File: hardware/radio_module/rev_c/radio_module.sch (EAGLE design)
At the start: 139 parts, among them J1 MOLEX_73251-135X, J10 TC2030-JLINK-L, J11 TC2030-JLINK-NL, J12 U.FL-R-SMT, J13 U.FL-R-SMT, J2 MOLEX_73251-135X, J3 NANO_SIM, J7 SIGNPOST_DEBUG_HEADERSMT, J8 SIGNPOST_MODULE_HEADER, J9 TC2030-JLINK-NL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

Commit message: fixed digikey part numbers
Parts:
- C10, C11, C12: DIGIKEY 490-6241-1-ND -> 490-6241-1-ND
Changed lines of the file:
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@@
 </part>
 <part name="C10" library="passives" deviceset="CAPACITOR" device="0402_CAP" value="47pF">
-<attribute name="DIGIKEY" value="490-6241-1-ND "/>
+<attribute name="DIGIKEY" value="490-6241-1-ND"/>
 </part>
 <part name="C11" library="passives" deviceset="CAPACITOR" device="0402_CAP" value="47pF">
-<attribute name="DIGIKEY" value="490-6241-1-ND "/>
+<attribute name="DIGIKEY" value="490-6241-1-ND"/>
 </part>
 <part name="C12" library="passives" deviceset="CAPACITOR" device="0402_CAP" value="47pF">
-<attribute name="DIGIKEY" value="490-6241-1-ND "/>
+<attribute name="DIGIKEY" value="490-6241-1-ND"/>
 </part>
 <part name="GND6" library="umich" deviceset="GND" device=""/>

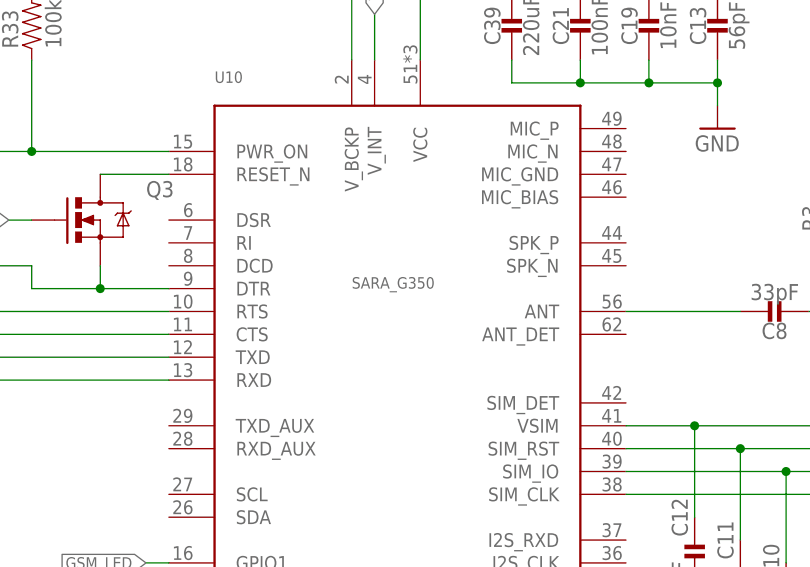
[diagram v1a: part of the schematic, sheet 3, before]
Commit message: added radio module with bom updates
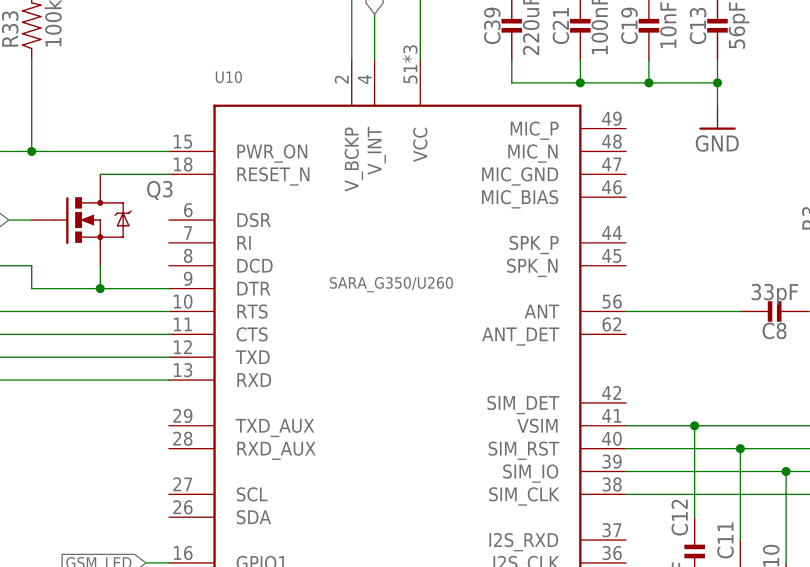
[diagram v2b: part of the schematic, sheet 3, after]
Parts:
- C1: DESCRIPTION (none) -> CAP CER 0.8PF 50V C0G/NP0 0402; MANUFACTURER (none) -> Murata; MPN (none) -> GRM1555C1HR80BA01D
- C10, C11, C12, C9: DESCRIPTION (none) -> CAP CER 47PF 50V C0G/NP0 0402; MANUFACTURER (none) -> Murata; MPN (none) -> GRM1555C1H470FA01D
- C13: DESCRIPTION (none) -> CAP CER 56PF 50V C0G/NP0 0402; DIGIKEY 490-1288-1-ND -> 490-1288-1-ND; MANUFACTURER (none) -> Murata; MPN (none) -> GRM1555C1H560JA01D
- C14, C15: DESCRIPTION (none) -> CAP CER 1000PF 50V X7R 0402; MANUFACTURER (none) -> Murata; MPN (none) -> GRM155R71H102KA01D
- C16: DESCRIPTION (none) -> CAP CER 2200PF 25V 10% X7R 0402; MANUFACTURER (none) -> Murata; MPN (none) -> GRM155R71E222KA01D
- C17, C18: DESCRIPTION (none) -> CAP CER 3300PF 50V 10% X7R 0402; MANUFACTURER (none) -> Murata; MPN (none) -> GRM155R71H332KA01D
- C19: DESCRIPTION (none) -> CAP CER 10000PF 50V 10% X7R 0402; DIGIKEY 490-4516-1-ND -> 490-4516-1-ND; MANUFACTURER (none) -> Murata; MPN (none) -> GRM155R71H103KA88D
- C2, C3: DESCRIPTION (none) -> CAP CER 8PF 50V C0G/NP0 0402; MANUFACTURER (none) -> Murata; MPN (none) -> GRM1555C1H8R0BA01D
- C20: DESCRIPTION (none) -> CAP CER 0.047UF 25V X7R 0402; MANUFACTURER (none) -> Murata; MPN (none) -> GRM155R71E473KA88D
- C21, C22, C23, C24, C25, C26, C27, C28, C29: DESCRIPTION (none) -> CAP CER 0.1UF 10V X7R 0402; MANUFACTURER (none) -> Murata; MPN (none) -> GRM155R71A104JA01D
- C30: DESCRIPTION (none) -> CAP CER 1UF 6.3V X5R 0402; MANUFACTURER (none) -> Murata; MPN (none) -> GRM155R60J105KE19D
- C31, C32: DESCRIPTION (none) -> CAP CER 4.7UF 10V X5R 0402; MANUFACTURER (none) -> Murata; MPN (none) -> ZRB15XR61A475KE01D
- C33, C34, C35: DESCRIPTION (none) -> CAP CER 10UF 6.3V X6S 0402; MANUFACTURER (none) -> Murata; MPN (none) -> GRM155C80J106ME11D
- C36, C37: DESCRIPTION (none) -> CAP CER 22UF 6.3V X5R 0402; DIGIKEY 1276-6834-1-ND -> 1276-6834-1-ND; MANUFACTURER (none) -> Samsung; MPN (none) -> CL05A226MQ5QUNC
- C38: DESCRIPTION (none) -> CAP CER 100UF 6.3V X5R 0805; MANUFACTURER (none) -> Murata; MPN (none) -> GRM21BR60J107ME15L
- C39: DESCRIPTION (none) -> CAP CER 220UF 6.3V X5R 1210; DIGIKEY 1276-3375-1-ND -> 1276-3375-1-ND; MANUFACTURER (none) -> Samsung; MPN (none) -> CL32A227MQVNNNE
- C4, C5, C6, C7: DESCRIPTION (none) -> CAP CER 12PF 50V C0G/NP0 0402; MANUFACTURER (none) -> Murata; MPN (none) -> GRM1555C1H120GA01D
- C8: DESCRIPTION (none) -> CAP CER 33PF 250V C0G/NP0 0603; MANUFACTURER (none) -> Johanson; MPN (none) -> 251R14S330JV4T
- D1, D2, D3, D4: DIGIKEY PESD0402-140CT-ND -> PESD0402-140CT-ND; MANUFACTURER (none) -> Littlefuse; MPN (none) -> PESD0402-140
- FB1: DESCRIPTION (none) -> FERRITE BEAD 1.5 KOHM 0402 1LN; MANUFACTURER (none) -> TDK; MPN (none) -> MMZ1005Y152CT000
- J4, J5: DESCRIPTION (none) -> DIL VERTICAL PC TAIL PIN HEADER; MANUFACTURER (none) -> Harwin; MPN (none) -> M20-9980446
- J6: DESCRIPTION (none) -> CONN HEADER 10POS .100 STR TIN; MANUFACTURER (none) -> FCI; MPN (none) -> 67997-410HLF
- L1: DESCRIPTION (none) -> FIXED IND 15NH 320MA 460 MOHM; MANUFACTURER (none) -> Taiyo Yuden; MPN (none) -> HK100515NJ-T
- L4: DESCRIPTION (none) -> FIXED IND 10UH 50MA 900 MOHM SMD; MANUFACTURER (none) -> Murata; MPN (none) -> LQM18FN100M00D
- LED1, LED2, LED3: MANUFACTURER (none) -> Rohm; MPN (none) -> SML-D12M8WT86
- Q1, Q2, Q3: DESCRIPTION (none) -> MOSFET N-CH 60V 0.115A SOT-23; MANUFACTURER (none) -> ON Semiconductor; MPN (none) -> 2N7002LT1G
- R1, R2, R3: DESCRIPTION (none) -> RES SMD 0 OHM JUMPER 1/16W 0402; MANUFACTURER (none) -> Yageo; MPN (none) -> RC0402JR-070RL
- R10: DESCRIPTION (none) -> RES SMD 150 OHM 1% 1/16W 0402; MANUFACTURER (none) -> Rohm; MPN (none) -> MCR01MRTF1500
- R11, R12, R13, R14, R15, R16: DESCRIPTION (none) -> RES SMD 1K OHM 5% 1/16W 0402; MANUFACTURER (none) -> Yageo; MPN (none) -> RC0402JR-071KL
- R17, R19, R20, R21, R22, R23, R24, R25, R26, R27, R28, R29, R30, R31: DESCRIPTION (none) -> RES SMD 10K OHM 5% 1/16W 0402; DIGIKEY 311-10KJRCT-ND -> 311-10KJRCT-ND; MANUFACTURER (none) -> Yageo; MPN (none) -> RC0402JR-0710KL
- R18: DESCRIPTION (none) -> RES SMD 10K OHM 5% 1/16W 0402; DIGIKEY 311-10KJRCT-ND -> 311-10KJRCT-ND; DNP DNP -> (none); MANUFACTURER (none) -> Yageo; MPN (none) -> RC0402JR-0710KL
- R32: MANUFACTURER (none) -> Rohm; MPN (none) -> MCR01MRTF1202
- R33, R34, R35, R36, R37, R38, R39, R40, R41: DESCRIPTION (none) -> RES SMD 100K OHM 1% 1/16W 0402; DIGIKEY 311-100KLRCT-ND -> 311-100KLRCT-ND; MANUFACTURER (none) -> Yageo; MPN (none) -> RC0402FR-07100KL
- R4: DESCRIPTION (none) -> RES SMD 15 MOHM 1% 1/4W 0603; DIGIKEY 408-1406-1-ND -> 408-1406-1-ND; MANUFACTURER (none) -> Susumu; MPN (none) -> RL0816T-R015-F
- R42: DIGIKEY P200KLCT-ND -> P200KLCT-ND; MANUFACTURER (none) -> Panasonic; MPN (none) -> ERJ-2RKF2003X
- R43: DESCRIPTION (none) -> RES SMD 240K OHM 5% 1/16W 0402; DIGIKEY YAG3291CT-ND -> YAG3291CT-ND; MANUFACTURER (none) -> Yageo; MPN (none) -> RC0402JR-07240KL
- R44: DIGIKEY YAG3228CT-ND -> YAG3228CT-ND; MANUFACTURER (none) -> Yageo; MPN (none) -> RC0402FR-07750KL
- R45: DESCRIPTION (none) -> RES SMD 750K OHM 1% 1/16W 0402; DIGIKEY YAG3228CT-ND -> YAG3228CT-ND; MANUFACTURER (none) -> Yageo; MPN (none) -> RC0402FR-07750KL
- R5: DESCRIPTION (none) -> RES SMD 430 MOHM 1% 1/6W 0402; DIGIKEY P.43AKCT-ND -> P.43AKCT-ND; MANUFACTURER (none) -> Panasonic; MPN (none) -> ERJ-2BQFR43X
- R6: DESCRIPTION (none) -> RES SMD 3.32 OHM 1% 1/16W 0402; DIGIKEY 541-3.32LLCT-ND -> 541-3.32LLCT-ND; MANUFACTURER (none) -> Vishay Dale; MPN (none) -> CRCW04023R32FKED
- R7, R8, R9: DESCRIPTION (none) -> RES SMD 100 OHM 1% 1/16W 0402; MANUFACTURER (none) -> Yageo; MPN (none) -> RC0402FR-07100RL
- X4: MANUFACTURER (none) -> TXC; MPN (none) -> 8Y-16.000MAAV-T
